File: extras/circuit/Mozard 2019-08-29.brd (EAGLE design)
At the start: 94 x 71.1 mm, 43 parts, among them J4 Headphone/Line Out, U2 LM386

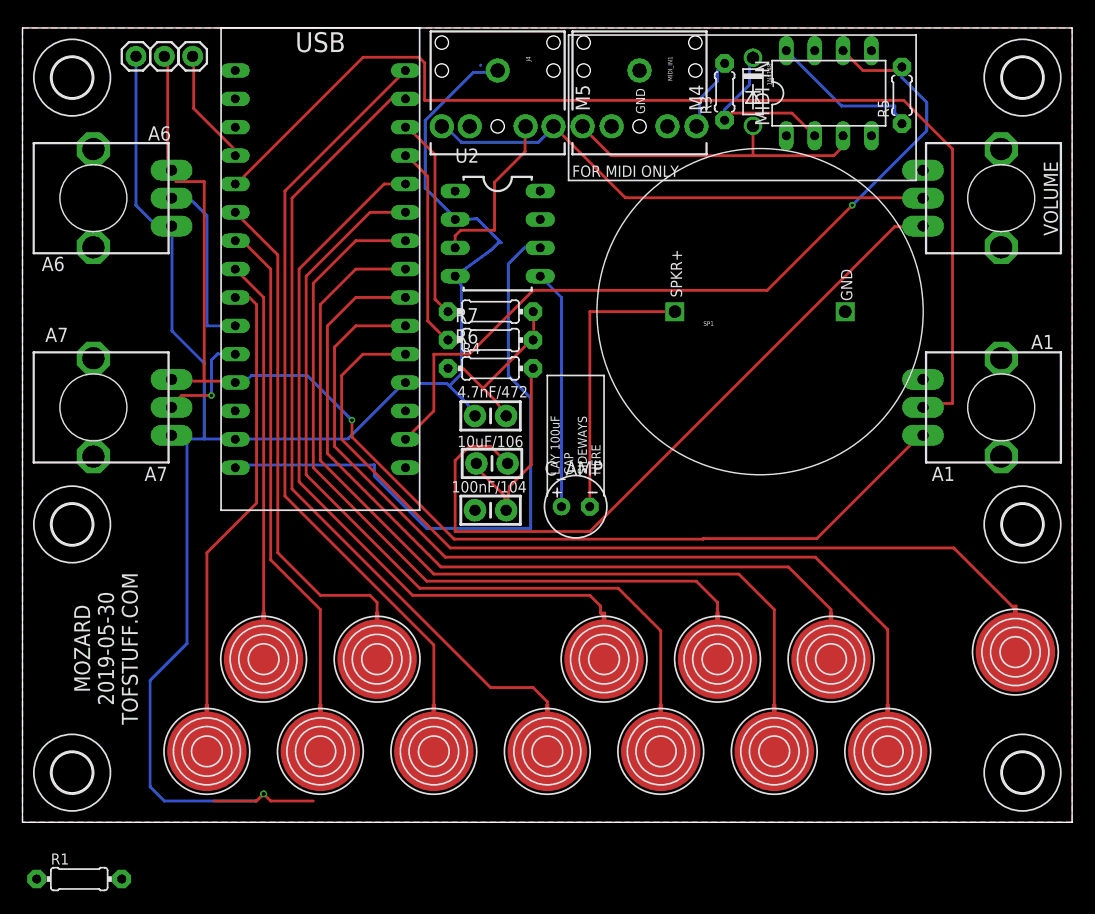
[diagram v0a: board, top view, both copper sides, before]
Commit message: Cap removed, resistor added
Big capacitor removed because it was useless. 100k resistor added between + and - of amp to cancel noise when jack plugged in.
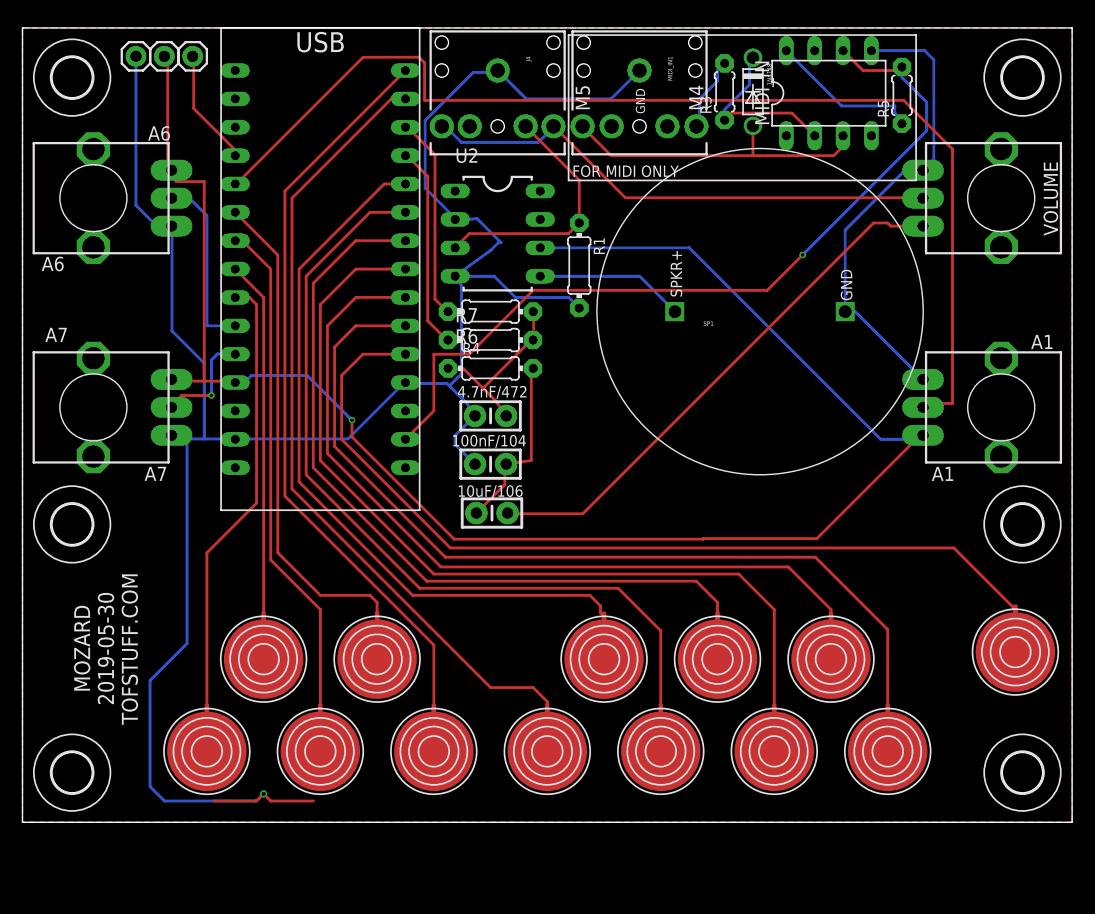
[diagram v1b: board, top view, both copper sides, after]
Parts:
- removed C_AMP: 100uF, TOF:E2,5-6
- moved R1 70.9 mm to (49.8, 49.8), turned to 270 degrees
- moved C2 4.45 mm to (42.0, 27.7)
- moved C4 4.13 mm to (41.9, 32.1)
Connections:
- removed net N$7: C_AMP.+, U2.5
- removed net V+: U$1.RAW, U2.6
- net N$1: now also U2.5; no longer C_AMP.-
- net VCC: now also U2.6
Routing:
- net GND: track 160.3 -> 235.4 mm
- net V+: track 57.4 -> 0.00 mm
- net VCC: track 110.9 -> 152.4 mm
- net N$7: track 21.4 -> 0.00 mm
- net N$2: track 65.4 -> 48.1 mm
- net N$1: track 25.1 -> 13.4 mm
- net N$6: track 15.2 -> 22.7 mm
- net N$4: track 19.0 -> 16.2 mm
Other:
- board text removed: "LAY 100uF CAP SIDEWAYS HERE"
